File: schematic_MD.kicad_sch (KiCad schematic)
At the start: 36 parts, among them J1 XT60, J11 CAN_Bus, J12 Micro_SD_Card_Det2, J2 XT60, J3 XT60, J4 CAN_Bus, J5 Rotaly_encoder_1, J6 Rotaly_encoder_2, J7 Conn_02x07_Odd_Even, J9 Conn_02x01, U11 74HC04, U7 MAX3051

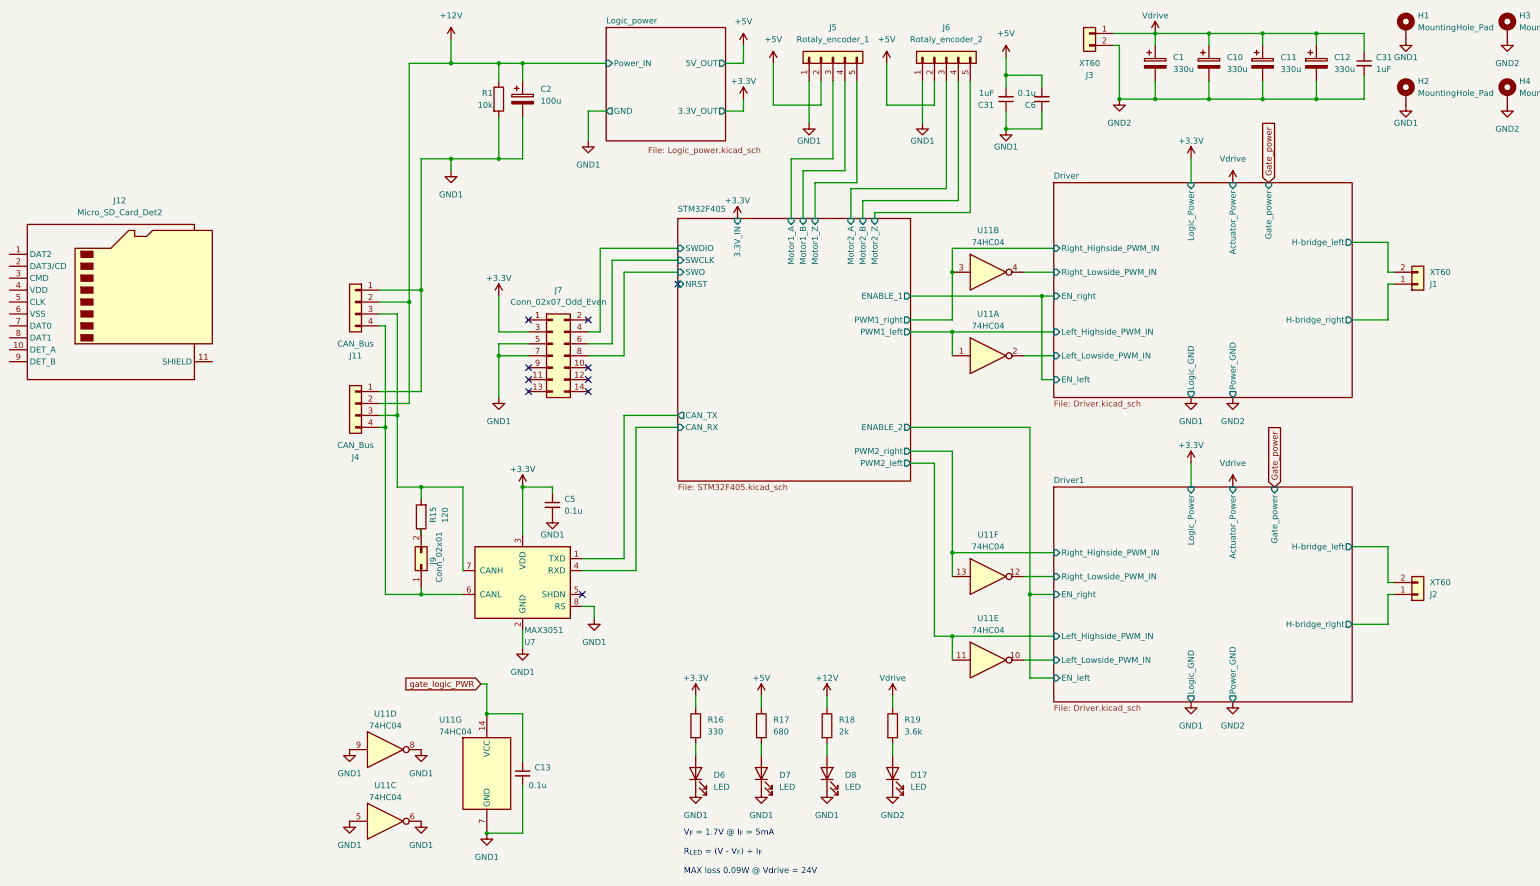
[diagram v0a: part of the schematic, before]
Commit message: Update PCB design & add microSD connector
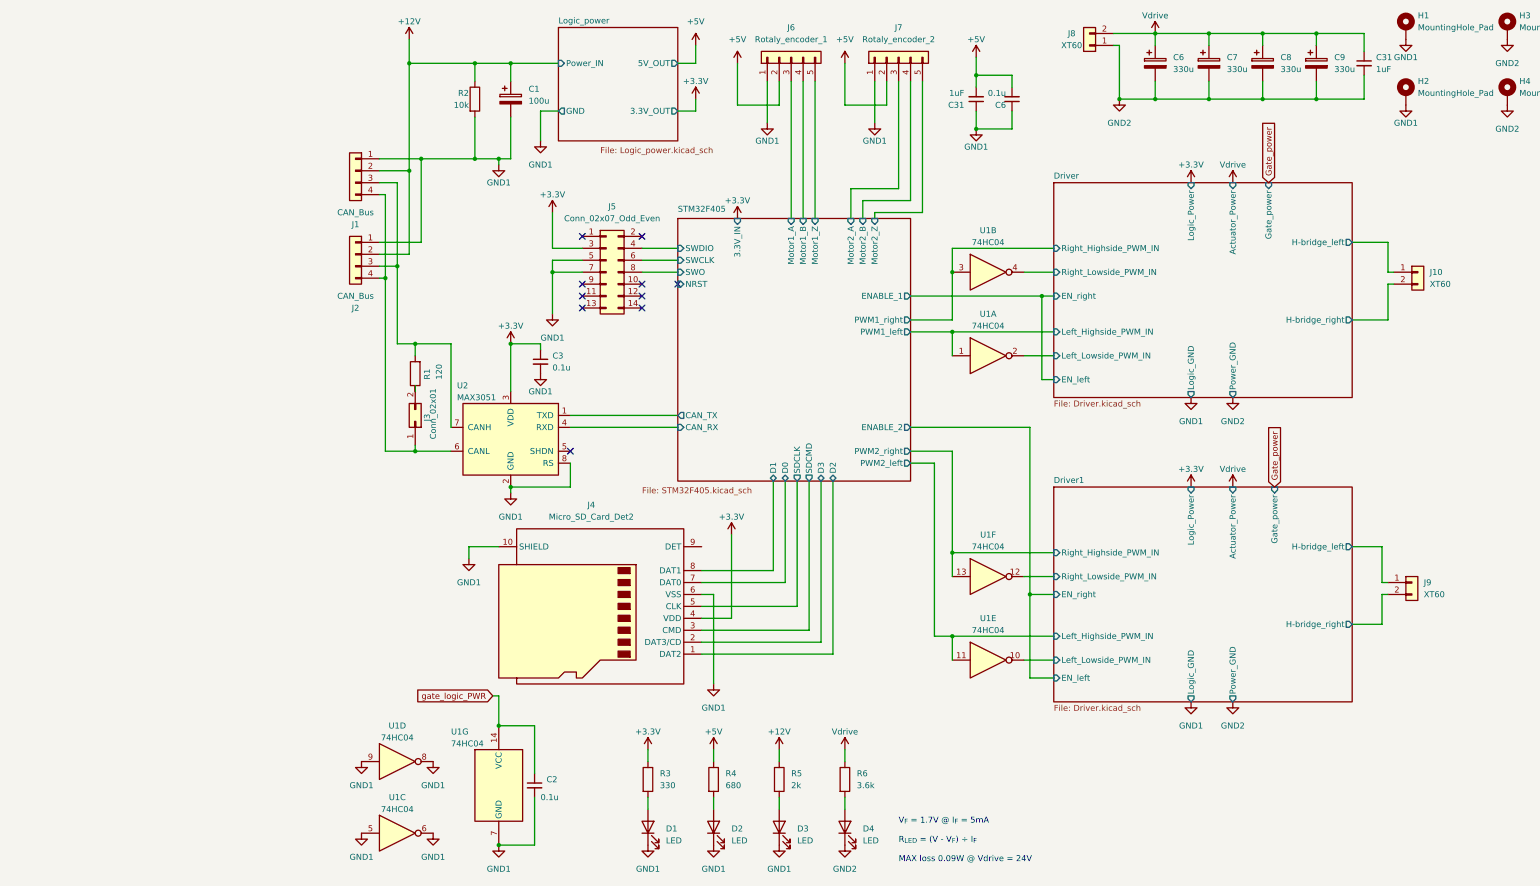
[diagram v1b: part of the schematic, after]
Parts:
- removed J2: XT60, Connector_AMASS:AMASS_XT60PW-F_1x02_P7.20mm_Horizontal, symbol Connector_Generic:Conn_01x02
- added J9: XT60, Connector_AMASS:AMASS_XT60PW-F_1x02_P7.20mm_Horizontal, symbol Connector_Generic:Conn_01x02
- C2: renamed from C13; footprint Capacitor_SMD:C_0402_1005Metric_Pad0.74x0.62mm_HandSolder -> Capacitor_SMD:C_0402_1005Metric
- C3: renamed from C5; footprint Capacitor_SMD:C_0402_1005Metric_Pad0.74x0.62mm_HandSolder -> Capacitor_SMD:C_0402_1005Metric
- C31, C6: footprint Capacitor_SMD:C_0603_1608Metric_Pad1.08x0.95mm_HandSolder -> Capacitor_SMD:C_0603_1608Metric
- D1: renamed from D6; footprint LED_SMD:LED_0603_1608Metric_Pad1.05x0.95mm_HandSolder -> LED_SMD:LED_0603_1608Metric
- D2: renamed from D7; footprint LED_SMD:LED_0603_1608Metric_Pad1.05x0.95mm_HandSolder -> LED_SMD:LED_0603_1608Metric
- D3: renamed from D8; footprint LED_SMD:LED_0603_1608Metric_Pad1.05x0.95mm_HandSolder -> LED_SMD:LED_0603_1608Metric
- D4: renamed from D17; footprint LED_SMD:LED_0603_1608Metric_Pad1.05x0.95mm_HandSolder -> LED_SMD:LED_0603_1608Metric
- J4: renamed from J12; footprint Connector_Card:microSD_HC_Molex_47219-2001 -> RDC_footprint:TF-15; symbol Connector:Micro_SD_Card_Det2 -> Connector:Micro_SD_Card_Det1
- R1: renamed from R15; footprint Resistor_SMD:R_0603_1608Metric_Pad0.98x0.95mm_HandSolder -> Resistor_SMD:R_0603_1608Metric
- R2: renamed from R1; footprint Resistor_SMD:R_1206_3216Metric_Pad1.30x1.75mm_HandSolder -> Resistor_SMD:R_1206_3216Metric
- R3: renamed from R16; footprint Resistor_SMD:R_0603_1608Metric_Pad0.98x0.95mm_HandSolder -> Resistor_SMD:R_0603_1608Metric
- R4: renamed from R17; footprint Resistor_SMD:R_0603_1608Metric_Pad0.98x0.95mm_HandSolder -> Resistor_SMD:R_0603_1608Metric
- R5: renamed from R18; footprint Resistor_SMD:R_0603_1608Metric_Pad0.98x0.95mm_HandSolder -> Resistor_SMD:R_0603_1608Metric
- R6: renamed from R19; footprint Resistor_SMD:R_0603_1608Metric_Pad0.98x0.95mm_HandSolder -> Resistor_SMD:R_0603_1608Metric
- U2: renamed from U7; footprint (none) -> Package_TO_SOT_SMD:SOT-23-8
- renumbered C2 to C1, C1 to C6, C10 to C7, C11 to C8, C12 to C9, J11 to J1, J1 to J10, J4 to J2, J9 to J3, J7 to J5, J5 to J6, J6 to J7, J3 to J8, U11 to U1
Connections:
- net +3.3V: now also J4.4 (VDD)
- net Driver/H-bridge_left: now also J10.1 (Pin_1); no longer J10.2 (Pin_2)
- net Driver/H-bridge_right: now also J10.2 (Pin_2); no longer J10.1 (Pin_1)
- net Driver1/H-bridge_left: now also J9.1 (Pin_1)
- net Driver1/H-bridge_right: now also J9.2 (Pin_2)
- net GND1: now also J4.10 (SHIELD), J4.6 (VSS)
- net GND2: now also J8.1 (Pin_1); no longer J8.2 (Pin_2)
- net Vdrive: now also J8.2 (Pin_2); no longer J8.1 (Pin_1)
- net STM32F405/D2: now reaches J4.1 (DAT2)
- net STM32F405/D3: now reaches J4.2 (DAT3/CD)
- net STM32F405/SDCMD: now reaches J4.3 (CMD)
- net STM32F405/SDCLK: now reaches J4.5 (CLK)
- net STM32F405/D0: now reaches J4.7 (DAT0)
- net STM32F405/D1: now reaches J4.8 (DAT1)
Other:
- sheet STM32F405 ports: added D0, D1, D2, D3, SDCLK, SDCMD; removed none
- moved on the sheet: C1, C2, C3, C31, C6, D1, D2, D3, D4, J1, J2, J3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

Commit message: add SEPIC IC symbol
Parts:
- added C6: 0.1u, Capacitor_SMD:C_0402_1005Metric, symbol Device:C_Small
- added R51, R52, R53, R54, R55: 10k, Resistor_SMD:R_0402_1005Metric, symbol Device:R
- added R56, R57, R58, R59, R60, R61: 0, Resistor_SMD:R_0402_1005Metric, symbol Device:R
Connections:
- net +3.3V: now also C6.2, R51.1, R52.1, R53.1, R54.1, R55.1
- net GND1: now also C6.1
- net STM32F405/D0: now also R57.1; no longer J4.7 (DAT0)
- net STM32F405/D1: now also R56.1; no longer J4.8 (DAT1)
- net STM32F405/D2: now also R61.1; no longer J4.1 (DAT2)
- net STM32F405/D3: now also R60.1; no longer J4.2 (DAT3/CD)
- net STM32F405/SDCLK: now also R58.1; no longer J4.5 (CLK)
- net STM32F405/SDCMD: now also R59.1; no longer J4.3 (CMD)
- new net: J4.1 (DAT2), R55.2, R61.2
- new net: J4.7 (DAT0), R52.2, R57.2
- new net: J4.2 (DAT3/CD), R54.2, R60.2
- new net: J4.3 (CMD), R53.2, R59.2
- new net: J4.5 (CLK), R58.2
- new net: J4.8 (DAT1), R51.2, R56.2
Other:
- moved on the sheet: C1, C2, C3, C31, C6, C7, C8, C9, D1, D2, D3, D4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

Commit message: minor change
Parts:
- removed J4: Micro_SD_Card_Det2, RDC_footprint:TF-15, symbol Connector:Micro_SD_Card_Det1
- added C60: 0.1u, Capacitor_SMD:C_0402_1005Metric, symbol Device:C_Small
- added J11: Micro_SD_Card_Det_Hirose_DM3AT, Connector_Card:microSD_HC_Hirose_DM3D-SF, symbol Connector:Micro_SD_Card_Det_Hirose_DM3AT
- added Q9: PMOS, symbol Simulation_SPICE:PMOS
- added R62, R63: 10k, Resistor_SMD:R_0402_1005Metric, symbol Device:R
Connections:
- net +12V: now also C60.1, Q9.3 (S), R63.1
- net +3.3V: now also J11.4 (VDD)
- net GND1: now also J11.11 (SHIELD), J11.6 (VSS), R62.2
- net at R55.2, R61.2: now also J11.1 (DAT2)
- net at R52.2, R57.2: now also J11.7 (DAT0)
- net at R54.2, R60.2: now also J11.2 (DAT3/CD)
- net at R53.2, R59.2: now also J11.3 (CMD)
- net at R58.2: now also J11.5 (CLK)
- net at R51.2, R56.2: now also J11.8 (DAT1)
- new net: C60.2, Q9.2 (G), R62.1, R63.2
- new net Logic_power/Power_IN: Q9.1 (D)
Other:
- moved on the sheet: C1, R2

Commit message: 制御回路完成
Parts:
- removed Q9: PMOS, symbol Simulation_SPICE:PMOS
- added C6: 0.1u, Capacitor_SMD:C_0603_1608Metric, symbol Device:C_Small
- added Q9: Q_PMOS_GSD, Package_TO_SOT_SMD:SOT-23-3, symbol Device:Q_PMOS_GSD
- added R10, R11, R12, R66, R9: 10k, Resistor_SMD:R_0402_1005Metric, symbol Device:R
- added SW2: SW_DIP_x04, Button_Switch_SMD:SW_DIP_SPSTx04_Slide_Copal_CHS-04B_W7.62mm_P1.27mm, symbol Switch:SW_DIP_x04
- added SW4: SW_SPDT, RDC_footprint:SS-12D, symbol Switch:SW_SPDT
- C1: value 100u -> 47u; footprint Capacitor_THT:CP_Radial_D6.3mm_P2.50mm -> Capacitor_THT:CP_Radial_D5.0mm_P2.00mm
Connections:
- net gate_logic_PWR is gone; now on net +3.3V: C2.1, U1.14 (VCC)
- net +12V: now also Q9.2 (S); no longer C1.1, R2.1
- net +3.3V: now also J11.9 (DET_B), SW2.5, SW2.6, SW2.7, SW2.8
- net +5V: now also C6.2
- net Driver/EN_left: now also U1.6
- net Driver1/EN_left: now also U1.8
- net GND1: now also C6.1, R10.2, R11.2, R12.2, R66.2, R9.2, SW4.3 (C); no longer H1.1, H2.1, R62.2, U1.5, U1.6, U1.8, U1.9
- net GND2: no longer H3.1, H4.1
- net Logic_power/Power_IN: now also C1.1, R2.1, Q9.3 (D)
- net at C60.2, R62.1, R63.2: now also Q9.1 (G)
- net SD_Detect: now reaches J11.10 (DET_A)
- net SD_Detect: now also R66.1
- new net: R62.2, SW4.2 (B)
- new net STM32F405/CAN_ID1: R9.1, SW2.1
- new net STM32F405/CAN_ID2: R10.1, SW2.2
- new net STM32F405/CAN_ID3: R11.1, SW2.3
- new net STM32F405/CAN_ID4: R12.1, SW2.4
- new net STM32F405/ENABLE_1: U1.5
- new net STM32F405/ENABLE_2: U1.9
- no-connect marks 10 -> 14
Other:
- added sheet Bootstrap_Power (24-12V_StepDown_DCDC.kicad_sch)
- sheet STM32F405 ports: added CAN_ID1, CAN_ID2, CAN_ID3, CAN_ID4, SD_Detector; removed none
- moved on the sheet: C3, C31, C6, C60, C7, C8, C9, H1, H2, H3, H4, J3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

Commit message: pre compleate
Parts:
- removed C31: 1uF, Capacitor_SMD:C_0603_1608Metric, symbol Device:C_Small
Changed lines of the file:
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@@
   (junction (at 148.59 173.99) (diameter 0) (color 0 0 0 0)
   )
-  (junction (at 342.9 36.83) (diameter 0) (color 0 0 0 0)
-  )
   (junction (at 154.94 212.09) (diameter 0) (color 0 0 0 0)
   )
@@
   )
   (junction (at 193.04 45.72) (diameter 0) (color 0 0 0 0)
-  )
-  (junction (at 342.9 22.86) (diameter 0) (color 0 0 0 0)
   )
   (junction (at 129.54 173.99) (diameter 0) (color 0 0 0 0)
@@
     (stroke (width 0) (type default))
   )
-  (wire (pts (xy 353.06 36.83) (xy 342.9 36.83))
-    (stroke (width 0) (type default))
-  )
   (wire (pts (xy 381 182.88) (xy 387.35 182.88))
     (stroke (width 0) (type default))
@@
     (stroke (width 0) (type default))
   )
-  (wire (pts (xy 353.06 26.67) (xy 353.06 22.86))
-    (stroke (width 0) (type default))
-  )
   (wire (pts (xy 58.42 101.6) (xy 67.31 101.6))
     (stroke (width 0) (type default))
@@
     (stroke (width 0) (type default))
   )
-  (wire (pts (xy 353.06 31.75) (xy 353.06 36.83))
-    (stroke (width 0) (type default))
-  )
   (wire (pts (xy 86.36 35.56) (xy 86.36 33.02))
     (stroke (width 0) (type default))
@@
   )
   (wire (pts (xy 203.2 152.4) (xy 203.2 226.06))
-    (stroke (width 0) (type default))
-  )
-  (wire (pts (xy 353.06 22.86) (xy 342.9 22.86))
     (stroke (width 0) (type default))
   )
@@
         )
       )
-    )
-  )
-  (symbol (lib_id "Device:C_Small") (at 353.06 29.21 0) (mirror y) (unit 1)
-    (in_bom yes) (on_board yes) (dnp no)
-    (property "Reference" "C31" (at 355.6 27.9463 0)
-      (effects (font (size 1.27 1.27)) (justify right))
-    )
-    (property "Value" "1uF" (at 355.6 30.48 0)
-      (effects (font (size 1.27 1.27)) (justify right))
-    )
-    (property "Footprint" "Capacitor_SMD:C_0603_1608Metric" (at 353.06 29.21 0)
-      (effects (font (size 1.27 1.27)) hide)
-    )
-    (property "Datasheet" "~" (at 353.06 29.21 0)
-      (effects (font (size 1.27 1.27)) hide)
-    )
-    (pin "1")
-    (pin "2")
-    (instances
-      (project "schematic_MD"
-        (path "/3152684b-d11f-4a9a-8e6c-09965044adbd/878f32b7-0d3d-4f49-a9dc-ebc0f2e1c793"
-          (reference "C31") (unit 1)
-        )
-        (path "/3152684b-d11f-4a9a-8e6c-09965044adbd"
-          (reference "C10") (unit 1)
-        )
-      )

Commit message: minor fix
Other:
- moved on the sheet: C1, C2, C3, C31, C6, C60, C7, C8, C9, D1, D2, D3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

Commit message: update BOM
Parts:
- C1: renamed from C60; value 0.1u -> 0.1uF; LCSC (none) -> C307331
- C10: renamed from C7; value 330u -> 330uF
- C11: renamed from C8; value 330u -> 330uF
- C12: renamed from C9; value 330u -> 330uF
- C2: renamed from C3; value 0.1u -> 0.1uF; LCSC (none) -> C307331
- C3: renamed from C1; value 47u -> 47uF
- C31: LCSC (none) -> C15849
- C5: renamed from C2; value 0.1u -> 0.1uF; LCSC (none) -> C307331
- C6: value 0.1u -> 0.1uF; LCSC (none) -> C14663
- C6: value 0.1u -> 0.1uF; LCSC (none) -> C307331
- C9: renamed from C6; value 330u -> 330uF
- D1, D2, D3, D4: LCSC (none) -> C2286
- J4: renamed from J11; LCSC (none) -> C719027
- Q1: renamed from Q9; FT Rotation Offset (none) -> 180; LCSC (none) -> C15127
- R1: LCSC (none) -> C22787
- R10: renamed from R52; LCSC (none) -> C25744
- R10, R11, R12, R9: LCSC (none) -> C25744
- R12: renamed from R53; LCSC (none) -> C25744
- R13: renamed from R54; LCSC (none) -> C25744
- R14: renamed from R55; LCSC (none) -> C25744
- R15: renamed from R56; LCSC (none) -> C17168
- R16: renamed from R57; LCSC (none) -> C17168
- R17: renamed from R58; LCSC (none) -> C17168
- R18: renamed from R59; LCSC (none) -> C17168
- R19: renamed from R60; LCSC (none) -> C17168
- R2: renamed from R63; LCSC (none) -> C25744
- R20: renamed from R61; LCSC (none) -> C17168
- R21: renamed from R3; LCSC (none) -> C23138
- R22: renamed from R4; LCSC (none) -> C23228
- R23: renamed from R5; LCSC (none) -> C22975
- R24: renamed from R6; LCSC (none) -> C22980
- R3: renamed from R62; LCSC (none) -> C25744
- R4: renamed from R2; LCSC (none) -> C17902
- R5: renamed from R66; LCSC (none) -> C25744
- R8: renamed from R51; LCSC (none) -> C25744
- U1: renamed from U2; LCSC (none) -> C112005
- U2: renamed from U1; FT Rotation Offset (none) -> -90; LCSC (none) -> C5590
- renumbered SW4 to SW1
